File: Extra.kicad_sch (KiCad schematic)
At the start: 39 parts, among them J1 Conn_02x18_Row_Letter_First, J2 Conn_01x02, J3 Conn_02x34_Odd_Even, U1 SY8113, U2 TP5108E23E-33, U3 SR9900, Y1 25MHz

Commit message: update
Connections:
- net DM: now also J3.37 (Pin_37)
- net DP: now also J3.35 (Pin_35)
- net GND: now also J3.10 (Pin_10), J3.12 (Pin_12), J3.17 (Pin_17), J3.18 (Pin_18), J3.2 (Pin_2), J3.23 (Pin_23), J3.24 (Pin_24), J3.30 (Pin_30), J3.33 (Pin_33), J3.36 (Pin_36), J3.39 (Pin_39), J3.4 (Pin_4), J3.44 (Pin_44), J3.50 (Pin_50), J3.52 (Pin_52), J3.54 (Pin_54), J3.55 (Pin_55), J3.56 (Pin_56), J3.57 (Pin_57), J3.58 (Pin_58), J3.6 (Pin_6), J3.63 (Pin_63)
- no-connect marks 12 -> 56
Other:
- moved on the sheet: J3

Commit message: add more
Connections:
- net +3.3VA is gone; now on net VDD33: C11.1, C9.1, FB1.2, R8.2, R9.2
- net GND: now also C21.1; no longer C21.2
- net VDD12: now also C21.2; no longer C21.1
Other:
- moved on the sheet: C21

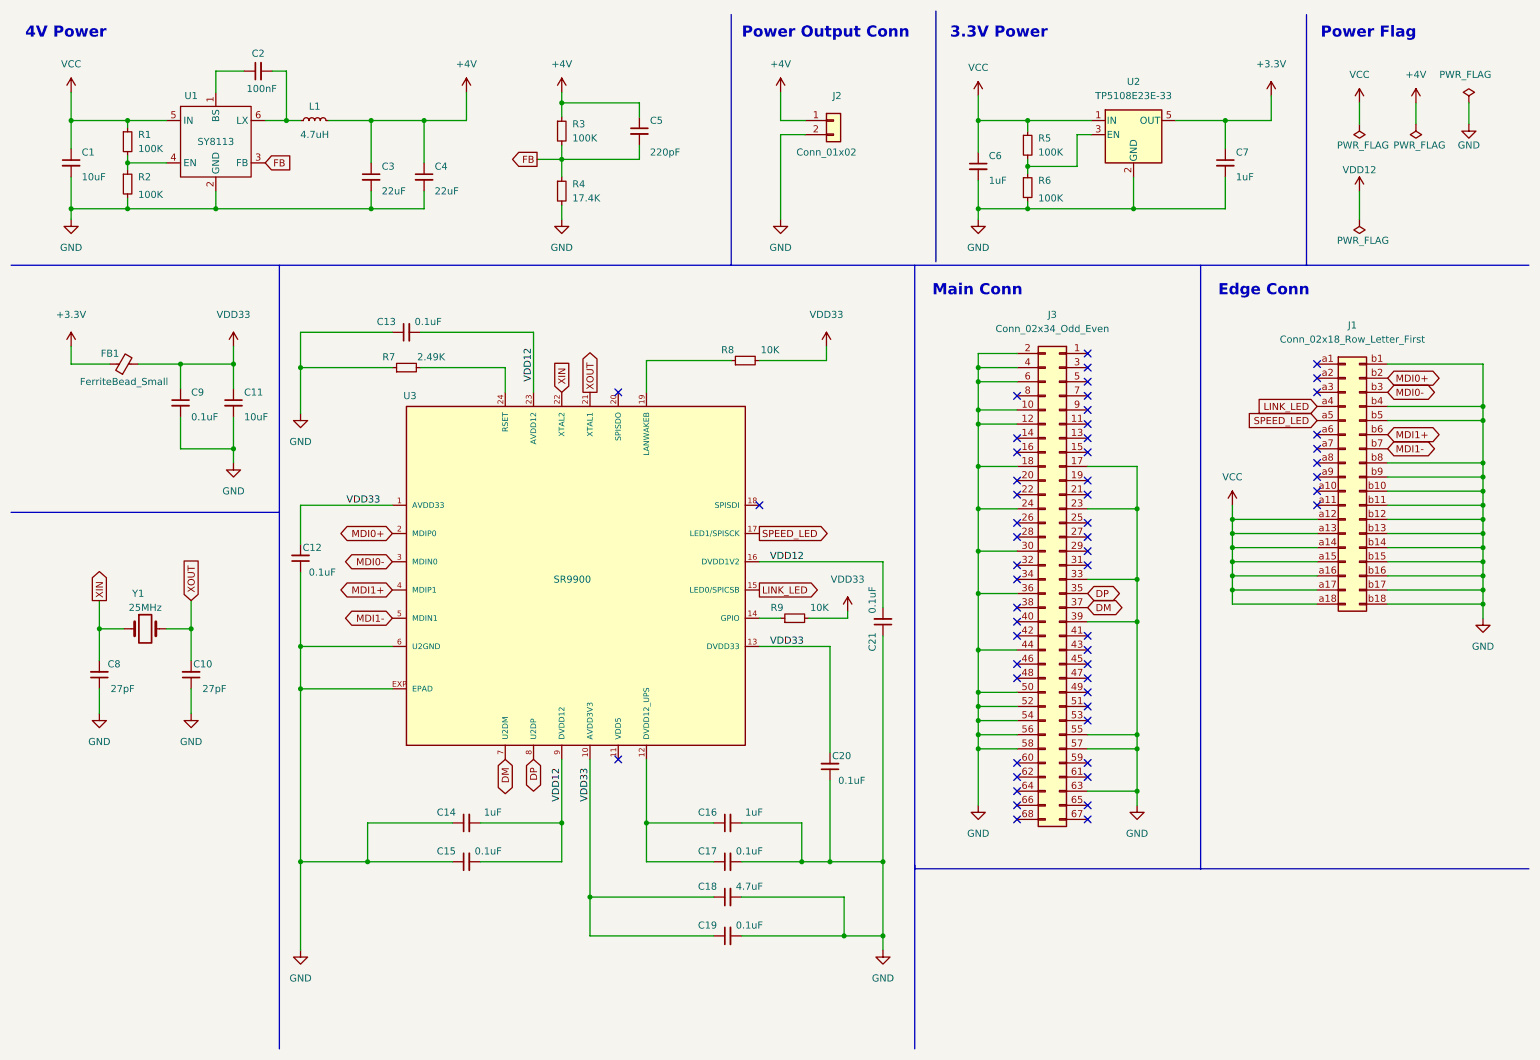
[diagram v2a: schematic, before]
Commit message: add common symbol to lib
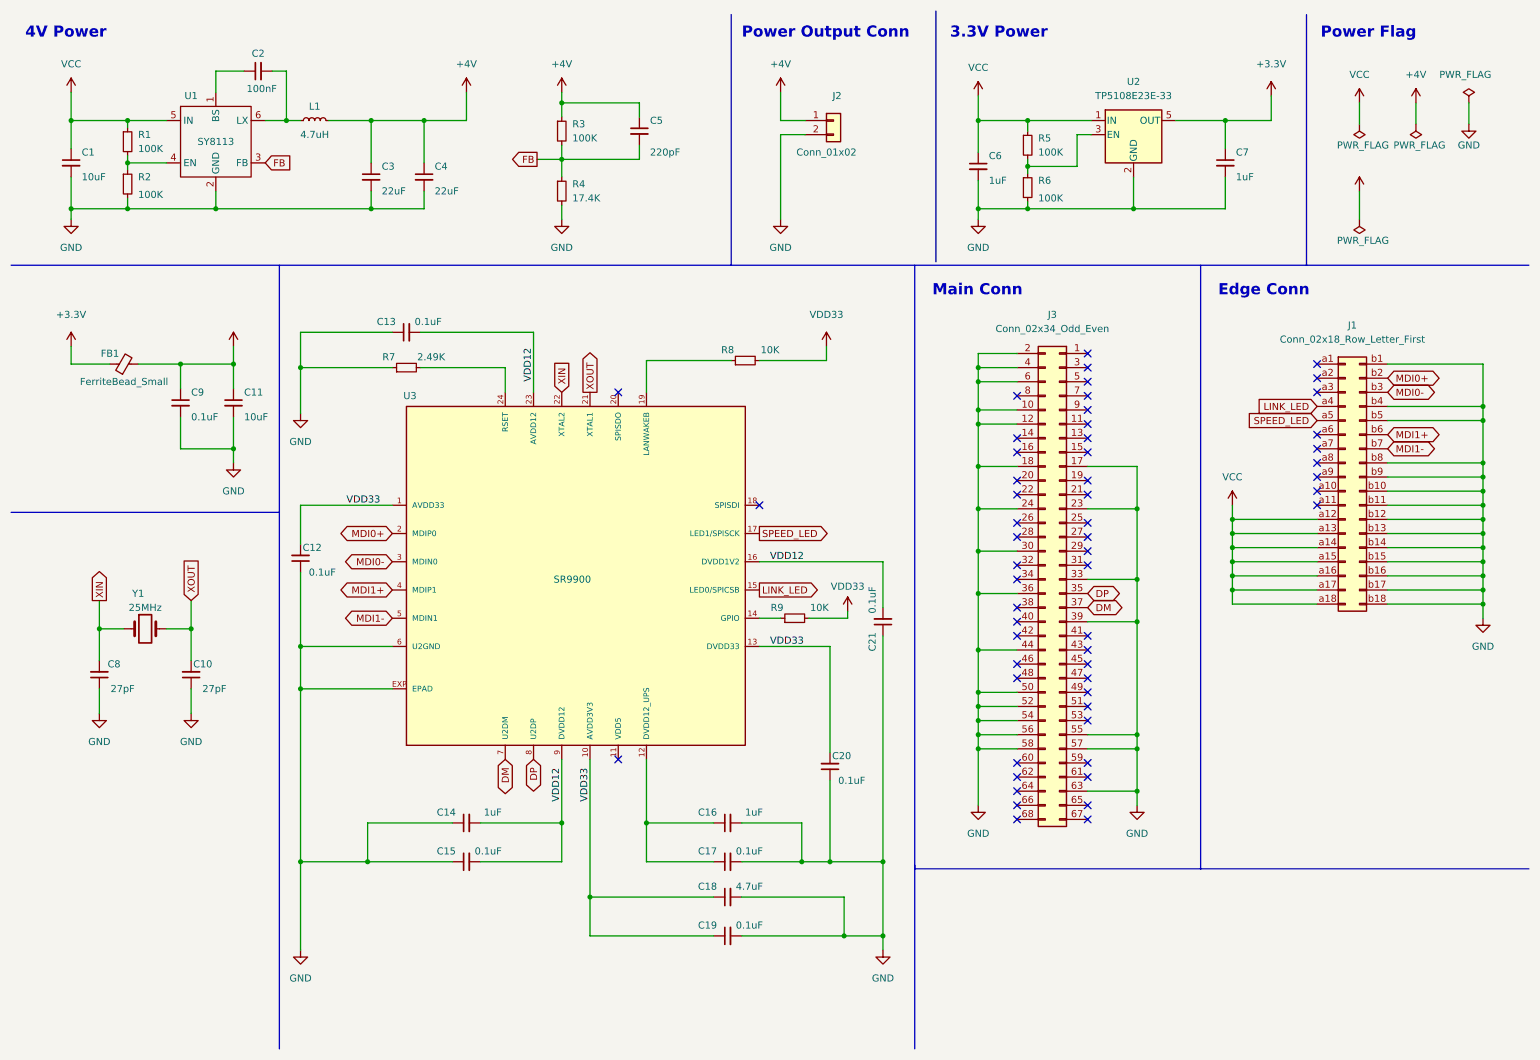
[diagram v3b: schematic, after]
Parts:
- U1: symbol Converter_DCDC:SY8113 -> USB_SR9900:SY8113
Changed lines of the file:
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@@
     (pin "2")
   )
-  (symbol (lib_id "power:VDD33") (at 162.56 116.84 0) (unit 1)
-    (in_bom no) (on_board no) (fields_autoplaced)
+  (symbol (lib_id "USB_SR9900:VDD33") (at 162.56 116.84 0) (unit 1)
+    (in_bom no) (on_board no)
     (property "Reference" "#PWR023" (id 0) (at 162.56 122.174 0)
       (effects (font (size 1.27 1.27)) hide)
     )
-    (property "Value" "VDD33" (id 1) (at 162.56 113.665 0))
+    (property "Value" "VDD33" (id 1) (at 162.56 114.935 0))
     (property "Footprint" "" (id 2) (at 162.56 116.84 0)
       (effects (font (size 1.27 1.27)) hide)
@@
     (pin "1")
   )
-  (symbol (lib_id "power:VDD33") (at 52.07 69.215 0) (unit 1)
+  (symbol (lib_id "USB_SR9900:VDD33") (at 52.07 69.215 0) (unit 1)
     (in_bom no) (on_board no) (fields_autoplaced)
     (property "Reference" "#PWR018" (id 0) (at 52.07 74.549 0)
       (effects (font (size 1.27 1.27)) hide)
     )
-    (property "Value" "VDD33" (id 1) (at 52.07 66.04 0))
+    (property "Value" "" (id 1) (at 52.07 66.04 0))
     (property "Footprint" "" (id 2) (at 52.07 69.215 0)
       (effects (font (size 1.27 1.27)) hide)
@@
     (pin "1")
     (pin "2")
+  )
+  (symbol (lib_id "USB_SR9900:VDD12") (at 254.635 41.275 0) (unit 1)
+    (in_bom yes) (on_board yes)
+    (property "Reference" "#PWR0104" (id 0) (at 254.635 45.847 0)
+      (effects (font (size 1.27 1.27)) hide)
+    )
+    (property "Value" "" (id 1) (at 254.635 39.37 0))
+    (property "Footprint" "" (id 2) (at 254.635 41.275 0)
+      (effects (font (size 1.27 1.27)) hide)
+    )
+    (property "Datasheet" "" (id 3) (at 254.635 41.275 0)
+      (effects (font (size 1.27 1.27)) hide)
+    )
+    (pin "1")
   )
   (symbol (lib_id "power:GND") (at 168.91 180.34 0) (unit 1)
@@
     (pin "2")
   )
-  (symbol (lib_id "power:VDD12") (at 254.635 41.275 0) (unit 1)
-    (in_bom yes) (on_board yes)
-    (property "Reference" "#PWR014" (id 0) (at 254.635 45.847 0)
-      (effects (font (size 1.27 1.27)) hide)
-    )
-    (property "Value" "VDD12" (id 1) (at 254.635 40.005 0))
-    (property "Footprint" "" (id 2) (at 254.635 41.275 0)
-      (effects (font (size 1.27 1.27)) hide)
-    )
-    (property "Datasheet" "" (id 3) (at 254.635 41.275 0)
-      (effects (font (size 1.27 1.27)) hide)
-    )
-    (pin "1")
-  )
   (symbol (lib_id "Device:C_Small") (at 140.97 164.465 90) (unit 1)
     (in_bom yes) (on_board yes)
@@
     (pin "2")
   )
-  (symbol (lib_id "Converter_DCDC:SY8113") (at 42.545 28.575 0) (unit 1)
+  (symbol (lib_id "USB_SR9900:SY8113") (at 42.545 28.575 0) (unit 1)
     (in_bom yes) (on_board yes)
     (property "Reference" "U1" (id 0) (at 44.45 26.67 0))
@@
     (pin "1")
   )
-  (symbol (lib_id "power:VDD33") (at 158.75 69.215 0) (unit 1)
+  (symbol (lib_id "USB_SR9900:VDD33") (at 158.75 69.215 0) (unit 1)
     (in_bom no) (on_board no) (fields_autoplaced)
     (property "Reference" "#PWR019" (id 0) (at 158.75 74.549 0)
@@
       (reference "#PWR013") (unit 1) (value "GND") (footprint "")
     )
-    (path "/aad8e8b5-2bac-4732-892f-880444ca50fd"
-      (reference "#PWR014") (unit 1) (value "VDD12") (footprint "")
-    )
     (path "/ab1950c1-ce2d-4268-8e23-4b16ca084582"
       (reference "#PWR015") (unit 1) (value "GND") (footprint "")
@@
       (reference "#PWR0103") (unit 1) (value "GND") (footprint "")
     )
+    (path "/79b24665-ac72-40a1-bf98-1c90306aadbb"
+      (reference "#PWR0104") (unit 1) (value "VDD12") (footprint "")
+    )
     (path "/9a3716c9-8fe3-4129-8950-1f29a54cc844"
